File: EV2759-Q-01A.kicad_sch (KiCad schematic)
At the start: 82 parts, among them M1 AM4417P, M2 2N7002, U1 MP2759GQ

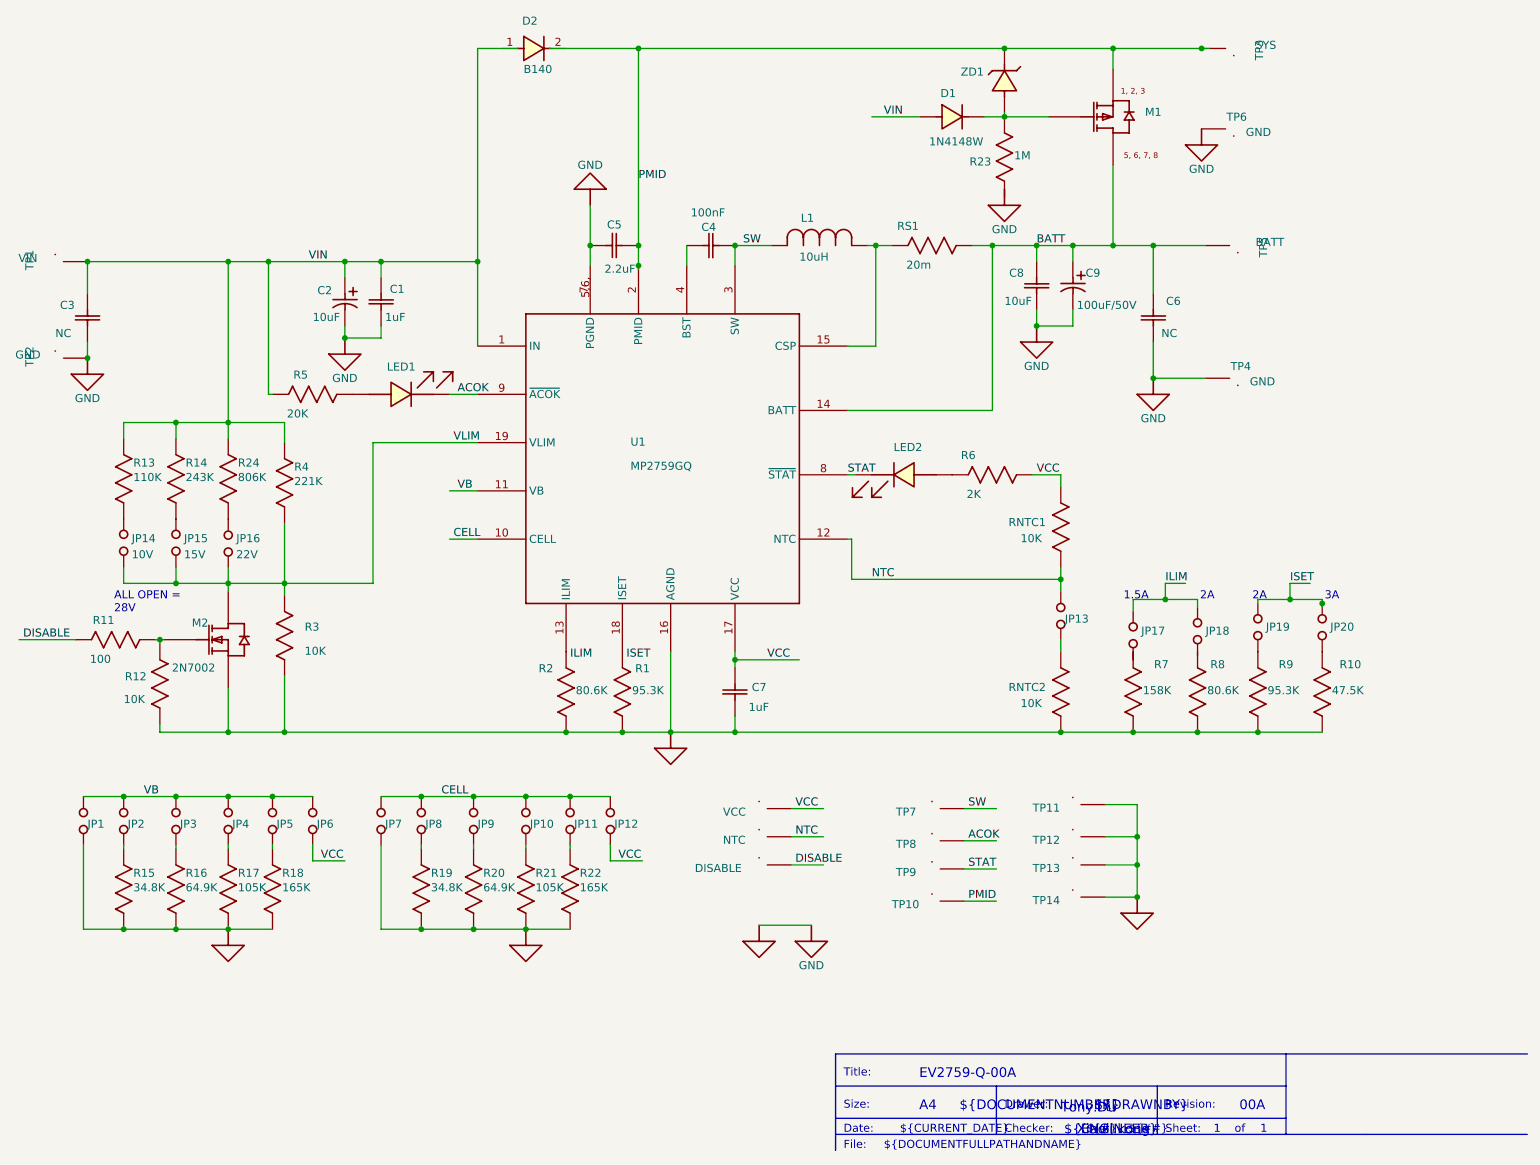
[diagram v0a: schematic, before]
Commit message: Switched main chip to supported model.
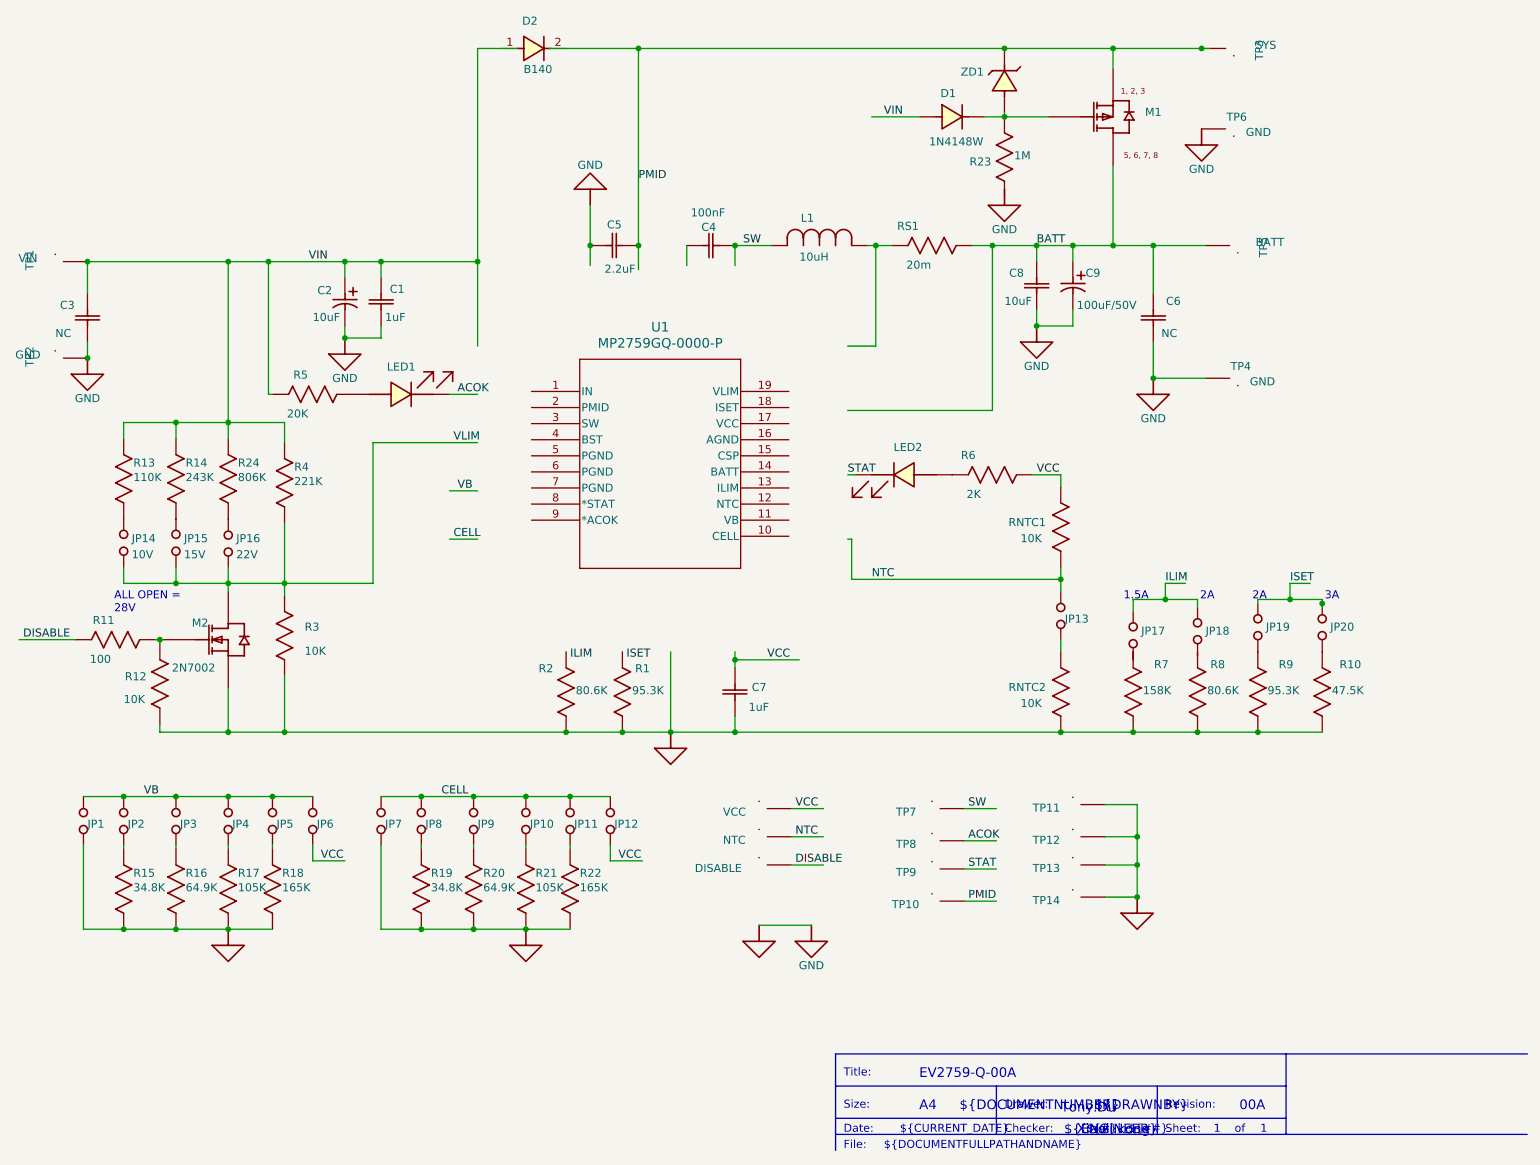
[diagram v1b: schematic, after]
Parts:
- removed U1: MP2759GQ, PCBComponent_1, symbol EV2759-Q-01A-altium-import:root_0_MP2759GQ
- added U1: MP2759GQ-0000-P, QFN-19_MP2759_MNP, symbol 2023-11-02_00-46-25:MP2759GQ-0000-P
